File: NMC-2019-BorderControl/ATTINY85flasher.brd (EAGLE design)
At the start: 52.5 x 52.5 mm, 17 parts, among them J1 ICSP-LO-SILK

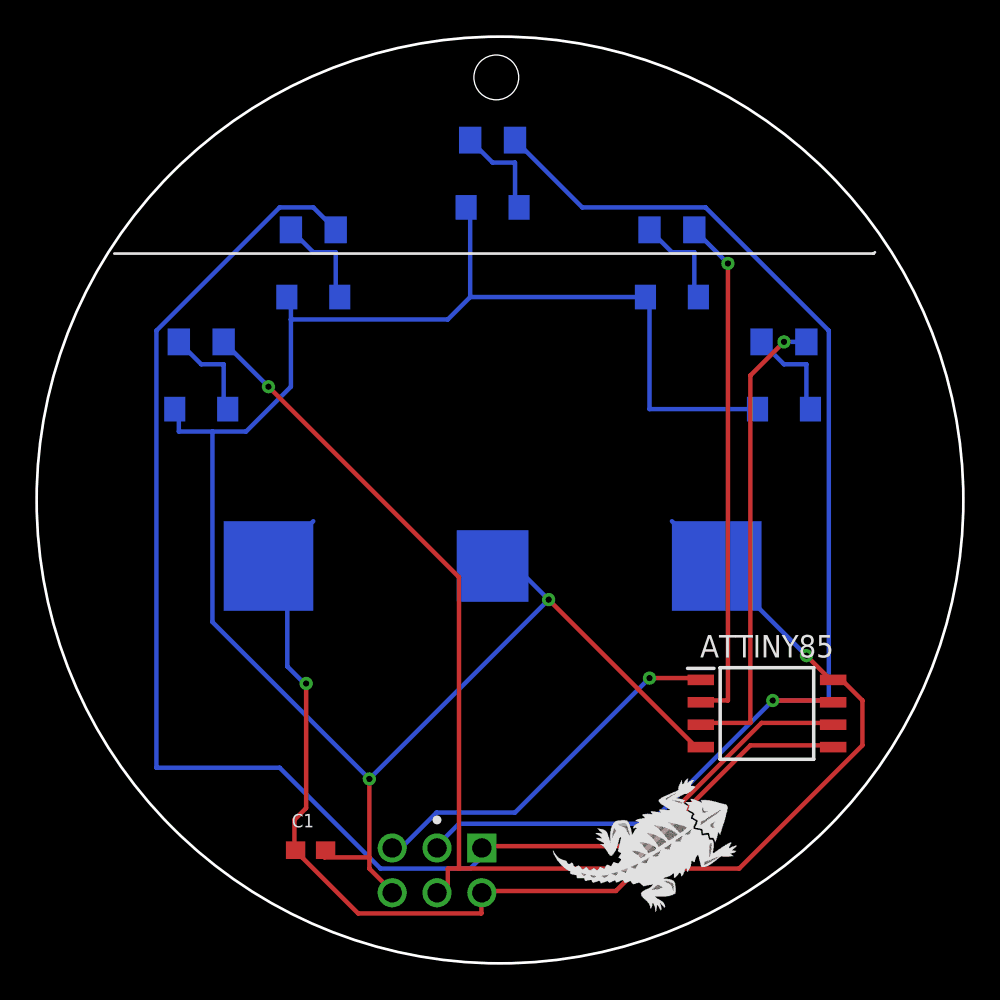
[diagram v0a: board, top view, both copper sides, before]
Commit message: added revB firmware and changed battery holder orientation
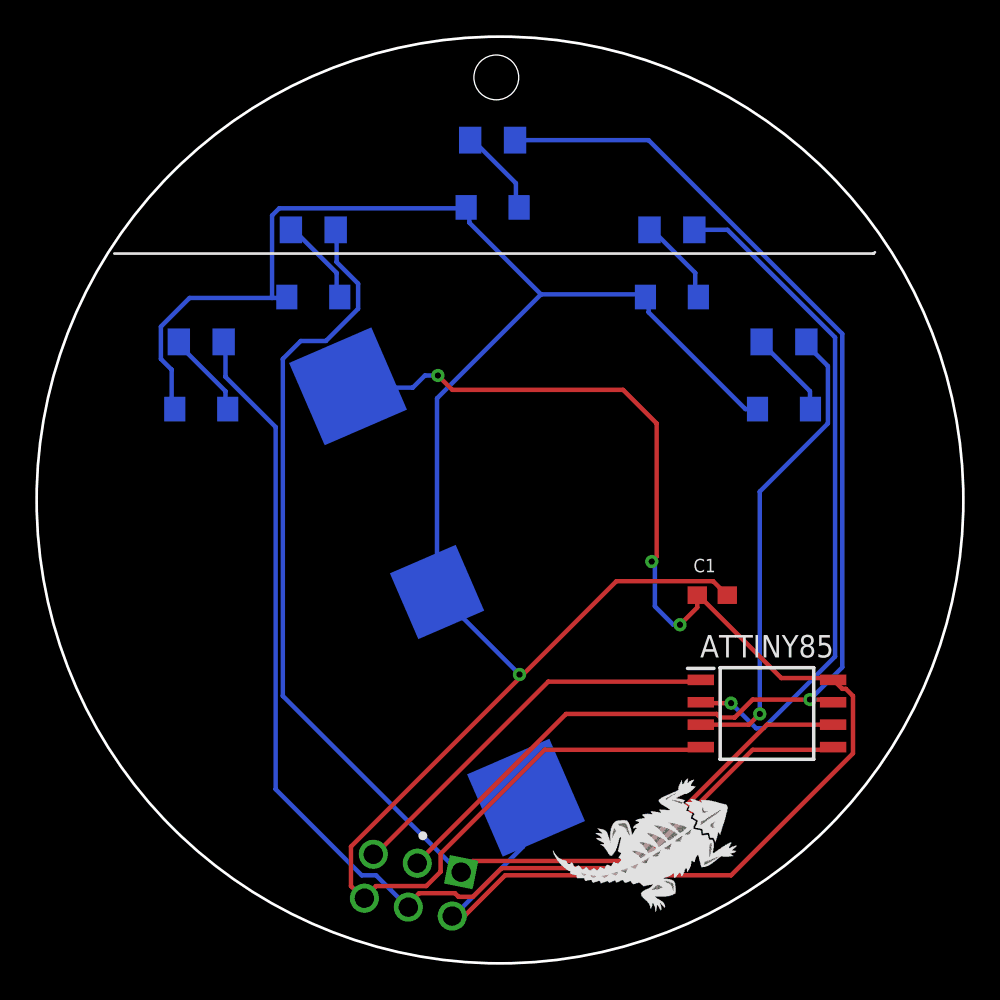
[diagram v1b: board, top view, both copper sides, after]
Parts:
- R1, R2, R3, R4, R5: value 56R -> 1.5k
- moved C1 27.0 mm to (35.3, 30.1)
- moved CR2032 3.48 mm to (19.7, 30.3), turned to 246.6 degrees
- moved J1 2.04 mm to (17.8, 11.2), turned to 348.5 degrees
- moved U$2 1.24 mm to (15.9, 18.0)
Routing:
- net GND: track 116.5 -> 131.5 mm, vias 2 -> 1
- net OUT1: track 82.7 -> 68.3 mm
- net OUT3: track 29.0 -> 38.5 mm
- net VCC: track 76.7 -> 83.0 mm, vias 2 -> 3
- net OUT0: track 62.0 -> 65.0 mm, vias 1 -> 0
- net RST: track 21.5 -> 22.6 mm, vias 1 -> 0
- net N$2: track 5.84 -> 4.96 mm
- net N$6: track 5.84 -> 5.03 mm
- net N$5: track 5.84 -> 5.06 mm
- net N$4: track 5.84 -> 5.06 mm
- net N$3: track 5.84 -> 5.06 mm
